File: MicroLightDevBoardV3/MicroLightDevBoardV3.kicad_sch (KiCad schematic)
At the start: 25 parts, among them J1 TYPE-C-31-M-12, J2 Conn_01x02_Socket, J3 Conn_01x03_Socket, SW1 SW_Push, U1 STM32C071GBUx, U2 S-85S1AB33-I6T1U, U4 BQ25180, U5 USBLC6-2P6

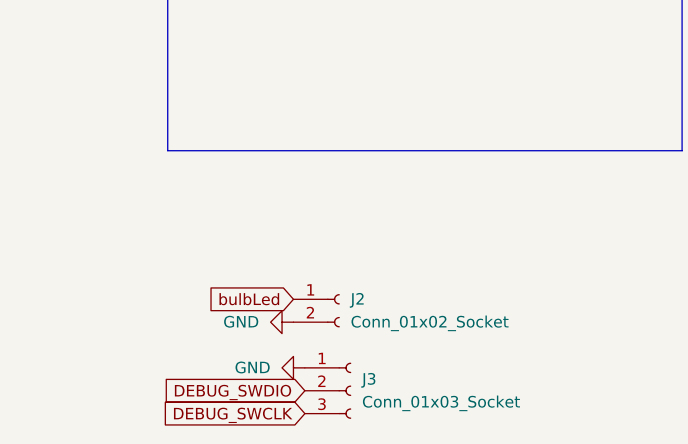
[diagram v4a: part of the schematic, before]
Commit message: remove lcsc ids, add some lcsc ids, add bulb led resistor
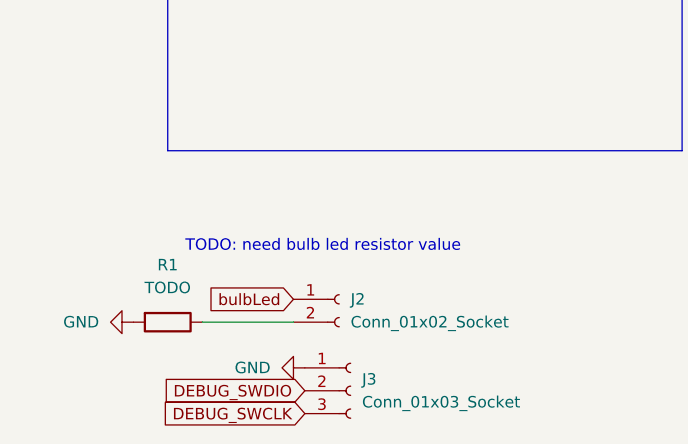
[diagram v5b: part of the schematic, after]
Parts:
- added R1: TODO, Resistor_SMD:R_0402_1005Metric, symbol Device:R
- C1, C3: LCSC C1712 -> (none)
- C2: LCSC C15850 -> (none)
- C4, C5: LCSC C96446 -> (none)
- R2: LCSC C23197 -> (none)
- R3, R4: LCSC C23140 -> (none)
- R5, R6: LCSC C23186 -> (none)
- SW1: LCSC (none) -> C455282
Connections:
- net GND: now also R1.2; no longer J2.2 (Pin_2)
- new net: J2.2 (Pin_2), R1.1
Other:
- note added: "TODO: need bulb led resistor value"
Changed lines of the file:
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@@
 		)
 	)
+	(text "TODO: need bulb led resistor value"
+		(exclude_from_sim no)
+		(at 50.292 169.418 0)
+		(effects
+			(font
+				(size 1.27 1.27)
+			)
+		)
+	)
 	(text "CaseLED\n"
 		(exclude_from_sim no)
@@
 	(wire
 		(pts
+			(xy 36.83 177.8) (xy 46.99 177.8)
+		)
+		(stroke
+			(width 0)
+			(type default)
+		)
+	)
+	(wire
+		(pts
 			(xy 93.98 26.67) (xy 92.71 26.67)
 		)
@@
 			)
 		)
-		(property "LCSC" "C15850"
-			(at 176.53 96.5199 0)
-			(effects
-				(font
-					(size 1.27 1.27)
-				)
-				(hide yes)
-			)
-		)
 		(pin "1"
 		)
@@
 			)
 		)
+		(property "LCSC" "C455282"
+			(at 113.03 172.72 0)
+			(effects
+				(font
+					(size 1.27 1.27)
+				)
+				(hide yes)
+			)
+		)
 		(pin "2"
 		)
@@
 	)
 	(symbol
+		(lib_id "Device:R")
+		(at 33.02 177.8 270)
+		(unit 1)
+		(exclude_from_sim no)
+		(in_bom yes)
+		(on_board yes)
+		(dnp no)
+		(property "Reference" "R1"
+			(at 33.02 171.45 90)
+			(effects
+				(font
+					(size 1.27 1.27)
+				)
+			)
+		)
+		(property "Value" "TODO"
+			(at 33.02 173.99 90)
+			(effects
+				(font
+					(size 1.27 1.27)
+				)
+			)
+		)
+		(property "Footprint" "Resistor_SMD:R_0402_1005Metric"
+			(at 33.02 176.022 90)
+			(effects
+				(font
+					(size 1.27 1.27)
+				)
+				(hide yes)
+			)
+		)
+		(property "Datasheet" "~"
+			(at 33.02 177.8 0)
+			(effects
+				(font
+					(size 1.27 1.27)
+				)
+				(hide yes)
+			)
+		)
+		(property "Description" "Resistor"
+			(at 33.02 177.8 0)
+			(effects
+				(font
+					(size 1.27 1.27)
+				)
+				(hide yes)
+			)
+		)
+		(pin "1"
+		)
+		(pin "2"
+		)
+		(instances
+			(project "MicroLightDevBoardV3"
+				(path "/9009d70b-273c-45fe-8624-596a22a35a49"
+					(reference "R1")
+					(unit 1)
+				)
+			)
+		)
+	)
+	(symbol
 		(lib_id "power:PWR_FLAG")
 		(at 236.22 91.44 270)
@@
 			)
 		)
-		(property "LCSC" "C23140"
-			(at 66.04 126.492 0)
-			(effects
-				(font
-					(size 1.27 1.27)
-				)
-				(hide yes)
-			)
-		)
 		(pin "2"
 		)
@@
 			)
 		)
-		(property "LCSC" "C1712"
-			(at 195.58 101.5999 0)
-			(effects
-				(font
-					(size 1.27 1.27)
-				)
-				(hide yes)
-			)
-		)
 		(pin "1"
 		)
@@
 			)
 		)
-		(property "LCSC" "C96446"
-			(at 163.83 58.4199 0)
-			(effects
-				(font
-					(size 1.27 1.27)
-				)
-				(hide yes)
-			)
-		)
 		(pin "1"
 		)
@@
 			)
 		)
-		(property "LCSC" "C23140"
-			(at 66.04 131.572 0)
-			(effects
-				(font
-					(size 1.27 1.27)
-				)
-				(hide yes)
-			)
-		)
 		(pin "2"
 		)
@@
 			)
 		)
-		(property "LCSC" "C1712"
-			(at 133.858 97.79 0)
-			(effects
-				(font
-					(size 1.27 1.27)
-				)
-				(hide yes)
-			)
-		)
 		(pin "1"
 		)
@@
 	(symbol
 		(lib_id "power:GND")
-		(at 46.99 177.8 270)
+		(at 29.21 177.8 270)
 		(unit 1)
 		(exclude_from_sim no)
@@
 		(fields_autoplaced yes)
 		(property "Reference" "#PWR05"
-			(at 40.64 177.8 0)
+			(at 22.86 177.8 0)
 			(effects
 				(font
@@
 		)
 		(property "Value" "GND"
-			(at 43.18 177.7999 90)
+			(at 25.4 177.7999 90)
 			(effects
 				(font
@@
 		)
 		(property "Footprint" ""
-			(at 46.99 177.8 0)
+			(at 29.21 177.8 0)
 			(effects
 				(font
@@
 		)
 		(property "Datasheet" ""
-			(at 46.99 177.8 0)
+			(at 29.21 177.8 0)
 			(effects
 				(font
@@
 		)
 		(property "Description" "Power symbol creates a global label with name \"GND\" , ground"
-			(at 46.99 177.8 0)
+			(at 29.21 177.8 0)
 			(effects
 				(font
@@
 			)
 		)
-		(property "LCSC" "C96446"
-			(at 236.22 60.9599 0)
-			(effects
-				(font
-					(size 1.27 1.27)
-				)
-				(hide yes)
-			)
-		)
 		(pin "1"
 		)
@@
 			)
 		)
-		(property "LCSC" "C23186"
-			(at 45.72 28.448 0)
-			(effects
-				(font
-					(size 1.27 1.27)
-				)
-				(hide yes)
-			)
-		)
 		(pin "2"
 		)
@@
 			)
 		)
-		(property "LCSC" "C23186"
-			(at 45.72 30.988 0)
-			(effects
-				(font
-					(size 1.27 1.27)
-				)
-				(hide yes)
-			)
-		)
 		(pin "2"
 		)
@@
 			(effects
 				(font
-					(size 1.27 1.27)
-				)
-				(hide yes)
-			)
-		)
-		(property "LCSC" "C23197"
-			(at 66.04 121.412 0)
-			(effects
-				(font

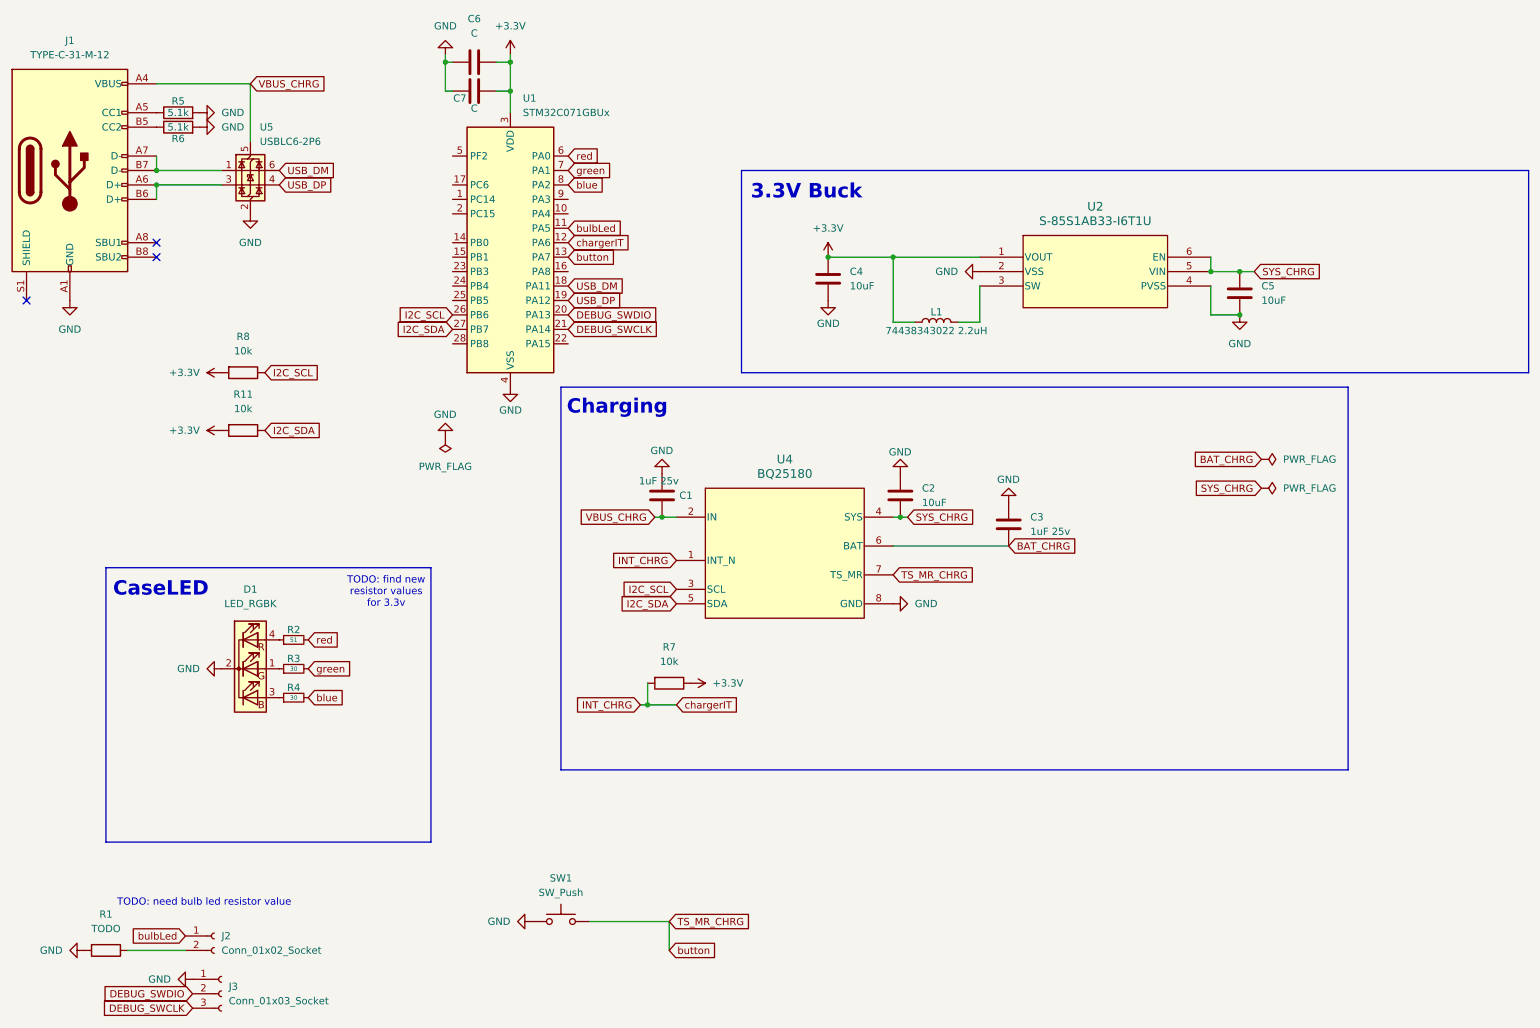
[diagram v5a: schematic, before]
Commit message: update led resistor value
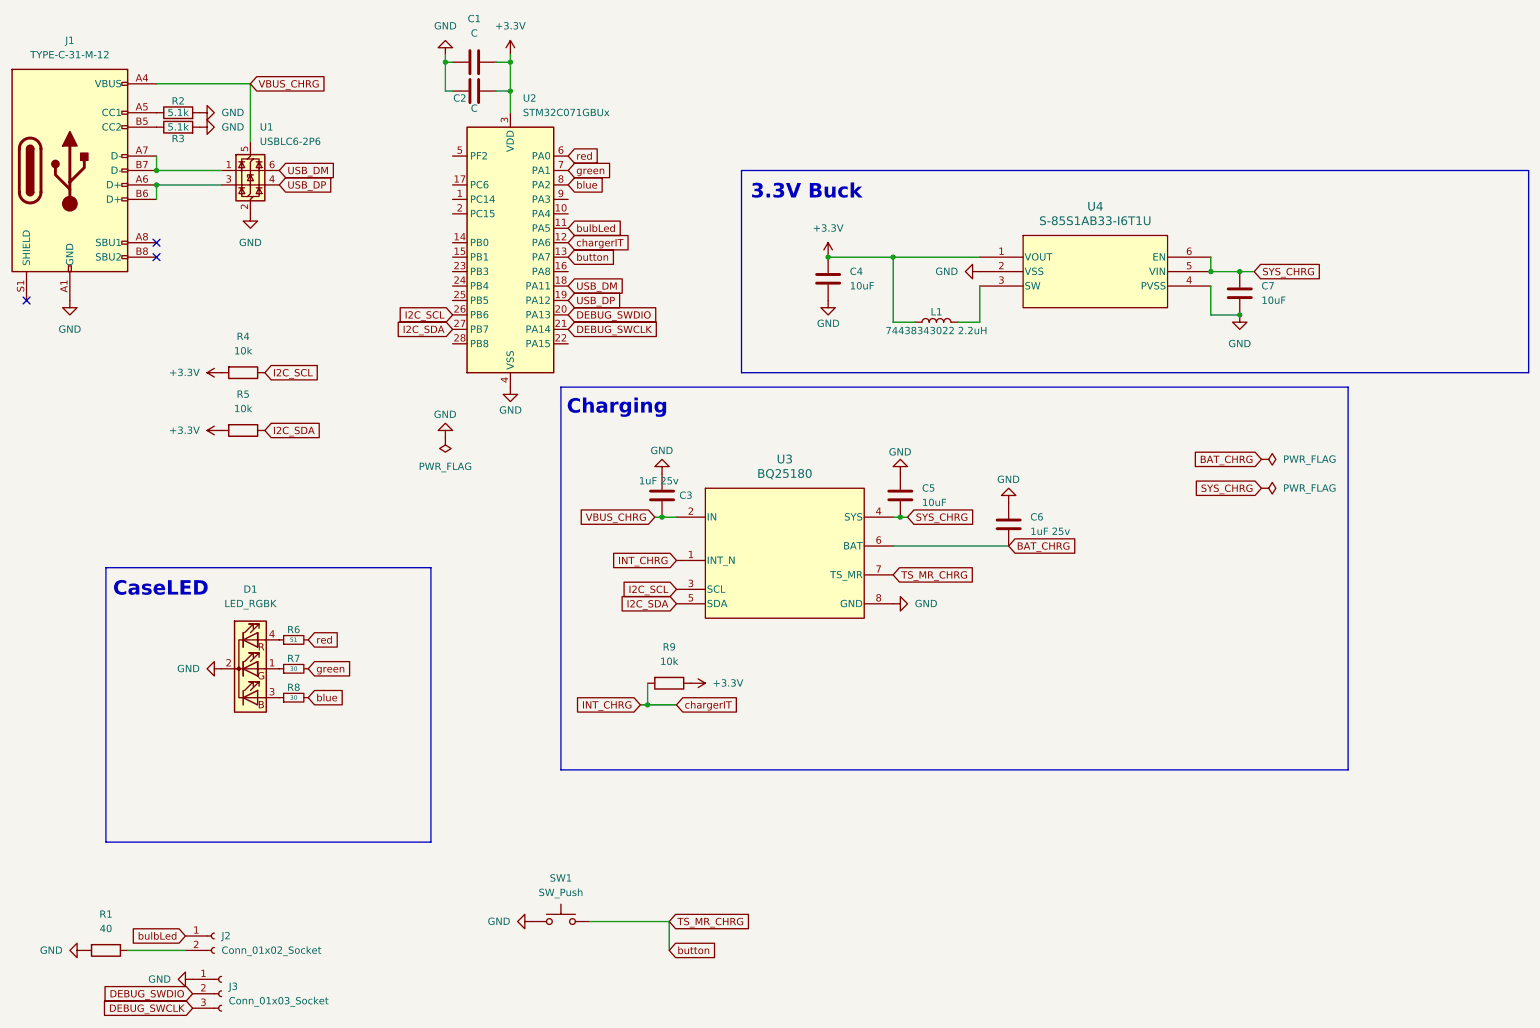
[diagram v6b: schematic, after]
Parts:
- R1: value TODO -> 40
- renumbered C6 to C1, C7 to C2, C1 to C3, C2 to C5, C3 to C6, C5 to C7, R5 to R2, R6 to R3, R8 to R4, R11 to R5, R2 to R6, R3 to R7, R4 to R8, R7 to R9, U5 to U1, U1 to U2, U4 to U3, U2 to U4
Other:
- note removed: "TODO: find new resistor values for 3.3v"
- note removed: "TODO: need bulb led resistor value"

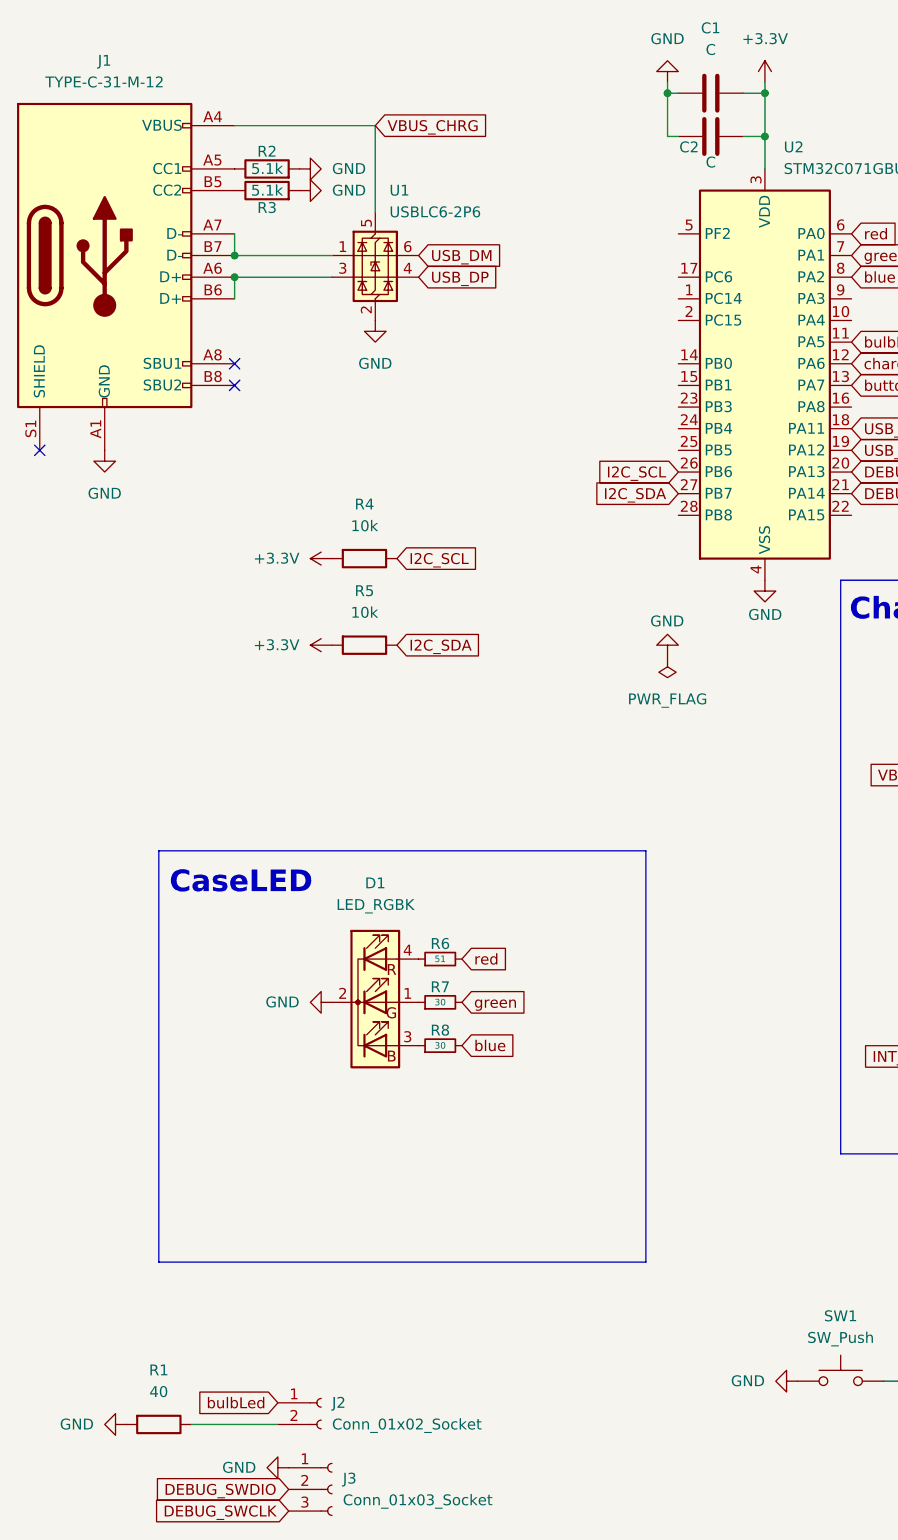
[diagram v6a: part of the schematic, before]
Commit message: add lcsc ids
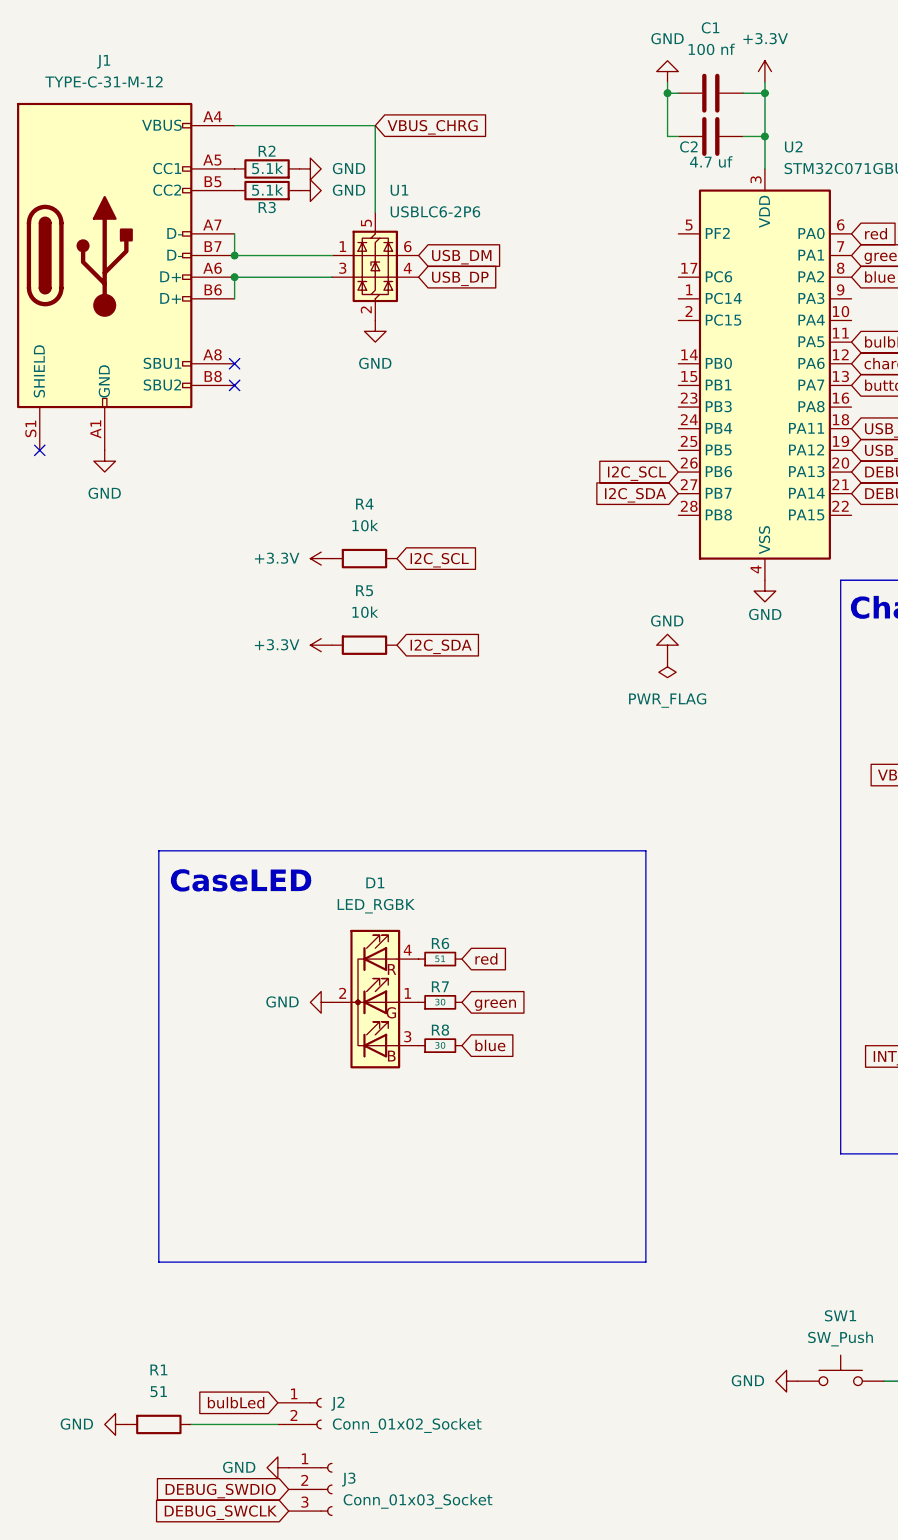
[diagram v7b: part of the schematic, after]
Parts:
- C1: value C -> 100 nf
- C2: value C -> 4.7 uf
- R1: value 40 -> 51
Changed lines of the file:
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@@
 			)
 		)
-		(property "Value" "40"
+		(property "Value" "51"
 			(at 33.02 173.99 90)
 			(effects
@@
 			)
 		)
-		(property "Value" "C"
+		(property "Value" "100 nf"
 			(at 97.79 16.51 90)
 			(effects
@@
 			)
 		)
-		(property "Value" "C"
+		(property "Value" "4.7 uf"
 			(at 97.79 29.718 90)
 			(effects
@@
 			(effects
 				(font
+					(size 1.27 1.27)
+				)
+				(hide yes)
+			)
+		)
+		(property "Field5" ""
+			(at 97.79 26.67 90)
+			(effects
+				(font

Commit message: silk screen cleanup
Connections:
- net bulbLed: now also J2.2 (Pin_2); no longer J2.1 (Pin_1)
- net at R1.1: now also J2.1 (Pin_1); no longer J2.2 (Pin_2)
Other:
- moved on the sheet: R1
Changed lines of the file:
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@@
 		)
 	)
-	(global_label "bulbLed"
+	(global_label "button"
 		(shape input)
-		(at 46.99 175.26 180)
+		(at 114.3 55.88 0)
 		(fields_autoplaced yes)
 		(effects
@@
 				(size 1.27 1.27)
 			)
-			(justify right)
+			(justify left)
 		)
 		(property "Intersheetrefs" "${INTERSHEET_REFS}"
-			(at 36.6269 175.26 0)
+			(at 123.3326 55.88 0)
 			(effects
 				(font
 					(size 1.27 1.27)
 				)
-				(justify right)
+				(justify left)
 				(hide yes)
 			)
 		)
 	)
-	(global_label "button"
+	(global_label "BAT_CHRG"
 		(shape input)
-		(at 114.3 55.88 0)
+		(at 191.77 106.68 0)
 		(fields_autoplaced yes)
 		(effects
@@
 		)
 		(property "Intersheetrefs" "${INTERSHEET_REFS}"
-			(at 123.3326 55.88 0)
+			(at 204.1895 106.68 0)
 			(effects
 				(font
@@
 		)
 	)
-	(global_label "BAT_CHRG"
+	(global_label "TS_MR_CHRG"
 		(shape input)
-		(at 191.77 106.68 0)
+		(at 171.45 111.76 0)
 		(fields_autoplaced yes)
 		(effects
@@
 		)
 		(property "Intersheetrefs" "${INTERSHEET_REFS}"
-			(at 204.1895 106.68 0)
+			(at 186.4094 111.76 0)
 			(effects
 				(font
@@
 		)
 	)
-	(global_label "TS_MR_CHRG"
+	(global_label "bulbLed"
 		(shape input)
-		(at 171.45 111.76 0)
+		(at 36.83 177.8 180)
 		(fields_autoplaced yes)
 		(effects
@@
 				(size 1.27 1.27)
 			)
-			(justify left)
+			(justify right)
 		)
 		(property "Intersheetrefs" "${INTERSHEET_REFS}"
-			(at 186.4094 111.76 0)
+			(at 26.4669 177.8 0)
 			(effects
 				(font
 					(size 1.27 1.27)
 				)
-				(justify left)
+				(justify right)
 				(hide yes)
 			)
@@
 	(symbol
 		(lib_id "Device:R")
-		(at 33.02 177.8 270)
+		(at 43.18 175.26 270)
 		(unit 1)
 		(exclude_from_sim no)
@@
 		(dnp no)
 		(property "Reference" "R1"
-			(at 33.02 171.45 90)
+			(at 43.18 168.91 90)
 			(effects
 				(font
@@
 		)
 		(property "Value" "51"
-			(at 33.02 173.99 90)
+			(at 43.18 171.45 90)
 			(effects
 				(font
@@
 		)
 		(property "Footprint" "Resistor_SMD:R_0402_1005Metric"
-			(at 33.02 176.022 90)
+			(at 43.18 173.482 90)
 			(effects
 				(font
@@
 		)
 		(property "Datasheet" "~"
-			(at 33.02 177.8 0)
+			(at 43.18 175.26 0)
 			(effects
 				(font
@@
 		)
 		(property "Description" "Resistor"
-			(at 33.02 177.8 0)
+			(at 43.18 175.26 0)
 			(effects
 				(font
@@
 	(symbol
 		(lib_id "power:GND")
-		(at 29.21 177.8 270)
+		(at 39.37 175.26 270)
 		(unit 1)
 		(exclude_from_sim no)
@@
 		(fields_autoplaced yes)
 		(property "Reference" "#PWR02"
-			(at 22.86 177.8 0)
+			(at 33.02 175.26 0)
 			(effects
 				(font
@@
 		)
 		(property "Value" "GND"
-			(at 25.4 177.7999 90)
+			(at 35.56 175.2599 90)
 			(effects
 				(font
@@
 		)
 		(property "Footprint" ""
-			(at 29.21 177.8 0)
+			(at 39.37 175.26 0)
 			(effects
 				(font
@@
 		)
 		(property "Datasheet" ""
-			(at 29.21 177.8 0)
+			(at 39.37 175.26 0)
 			(effects
 				(font
@@
 		)
 		(property "Description" "Power symbol creates a global label with name \"GND\" , ground"
-			(at 29.21 177.8 0)
+			(at 39.37 175.26 0)
 			(effects
 				(font
